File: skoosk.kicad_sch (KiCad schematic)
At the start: 99 parts, among them SW1 SW_Push, SW2 RotaryEncoder_Switch, U1 ProMicro

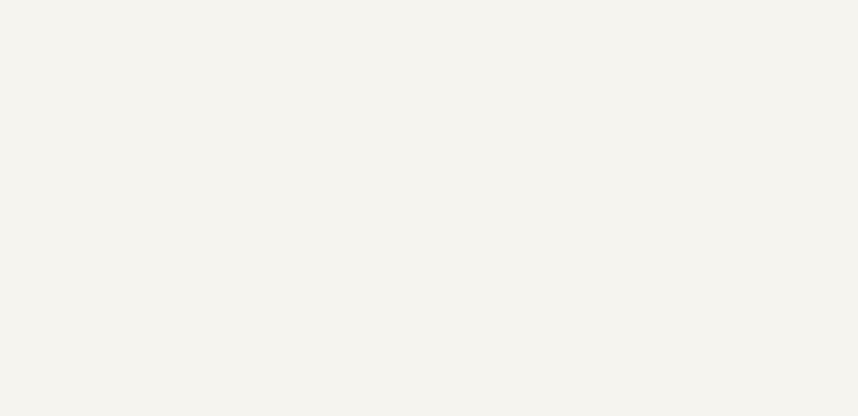
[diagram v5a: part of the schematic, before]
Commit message: mounting holes added
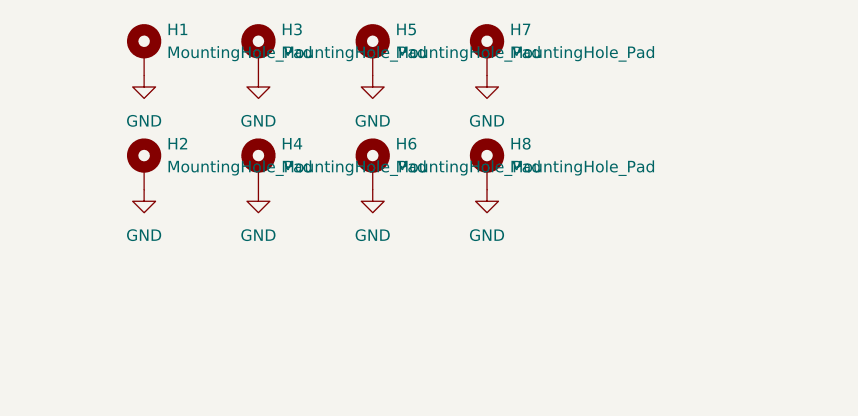
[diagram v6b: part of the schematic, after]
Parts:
- added H1, H2, H3, H4, H5, H6, H7, H8: MountingHole_Pad, MountingHole:MountingHole_2.7mm_M2.5_Pad, symbol Mechanical:MountingHole_Pad
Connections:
- net GND: now also H1.1, H2.1, H3.1, H4.1, H5.1, H6.1, H7.1, H8.1

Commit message: cleaned up pcb, switch & backplate
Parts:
- H1, H2, H3, H4, H5, H6, H7, H8: footprint MountingHole:MountingHole_2.7mm_M2.5_Pad -> MountingHole:MountingHole_2.2mm_M2_Pad
- Rrgb1: footprint Resistor_THT:R_Axial_DIN0204_L3.6mm_D1.6mm_P5.08mm_Horizontal -> Resistor_SMD:R_0603_1608Metric
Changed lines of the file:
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@@
       (effects (font (size 1.27 1.27)) (justify left))
     )
-    (property "Footprint" "MountingHole:MountingHole_2.7mm_M2.5_Pad" (id 2) (at 25.4 22.86 0)
+    (property "Footprint" "MountingHole:MountingHole_2.2mm_M2_Pad" (id 2) (at 25.4 22.86 0)
       (effects (font (size 1.27 1.27)) hide)
     )
@@
       (effects (font (size 1.27 1.27)) (justify left))
     )
-    (property "Footprint" "MountingHole:MountingHole_2.7mm_M2.5_Pad" (id 2) (at 50.8 22.86 0)
+    (property "Footprint" "MountingHole:MountingHole_2.2mm_M2_Pad" (id 2) (at 50.8 22.86 0)
       (effects (font (size 1.27 1.27)) hide)
     )
@@
       (effects (font (size 1.27 1.27)) (justify left))
     )
-    (property "Footprint" "MountingHole:MountingHole_2.7mm_M2.5_Pad" (id 2) (at 50.8 35.56 0)
+    (property "Footprint" "MountingHole:MountingHole_2.2mm_M2_Pad" (id 2) (at 50.8 35.56 0)
       (effects (font (size 1.27 1.27)) hide)
     )
@@
       (effects (font (size 1.27 1.27)) (justify left))
     )
-    (property "Footprint" "MountingHole:MountingHole_2.7mm_M2.5_Pad" (id 2) (at 38.1 35.56 0)
+    (property "Footprint" "MountingHole:MountingHole_2.2mm_M2_Pad" (id 2) (at 38.1 35.56 0)
       (effects (font (size 1.27 1.27)) hide)
     )
@@
       (effects (font (size 1.27 1.27)) (justify left))
     )
-    (property "Footprint" "MountingHole:MountingHole_2.7mm_M2.5_Pad" (id 2) (at 38.1 22.86 0)
+    (property "Footprint" "MountingHole:MountingHole_2.2mm_M2_Pad" (id 2) (at 38.1 22.86 0)
       (effects (font (size 1.27 1.27)) hide)
     )
@@
       (effects (font (size 1.27 1.27)) (justify left))
     )
-    (property "Footprint" "MountingHole:MountingHole_2.7mm_M2.5_Pad" (id 2) (at 63.5 22.86 0)
+    (property "Footprint" "MountingHole:MountingHole_2.2mm_M2_Pad" (id 2) (at 63.5 22.86 0)
       (effects (font (size 1.27 1.27)) hide)
     )
@@
       (effects (font (size 1.27 1.27)) (justify left))
     )
-    (property "Footprint" "MountingHole:MountingHole_2.7mm_M2.5_Pad" (id 2) (at 25.4 35.56 0)
+    (property "Footprint" "MountingHole:MountingHole_2.2mm_M2_Pad" (id 2) (at 25.4 35.56 0)
       (effects (font (size 1.27 1.27)) hide)
     )
@@
       (effects (font (size 1.27 1.27)) (justify left))
     )
-    (property "Footprint" "MountingHole:MountingHole_2.7mm_M2.5_Pad" (id 2) (at 63.5 35.56 0)
+    (property "Footprint" "MountingHole:MountingHole_2.2mm_M2_Pad" (id 2) (at 63.5 35.56 0)
       (effects (font (size 1.27 1.27)) hide)
     )
@@
       (effects (font (size 1.27 1.27)) (justify left))
     )
-    (property "Footprint" "Resistor_THT:R_Axial_DIN0204_L3.6mm_D1.6mm_P5.08mm_Horizontal" (id 2) (at 30.48 91.44 0)
+    (property "Footprint" "Resistor_SMD:R_0603_1608Metric" (id 2) (at 30.48 91.44 0)
       (effects (font (size 1.27 1.27)) hide)
     )
@@
     )
     (path "/1f47bf57-554a-4b3f-afe2-fbac827e2ba5"
-      (reference "H1") (unit 1) (value "MountingHole_Pad") (footprint "MountingHole:MountingHole_2.7mm_M2.5_Pad")
+      (reference "H1") (unit 1) (value "MountingHole_Pad") (footprint "MountingHole:MountingHole_2.2mm_M2_Pad")
     )
     (path "/af553349-715c-4608-b748-a1575ed68db3"
-      (reference "H2") (unit 1) (value "MountingHole_Pad") (footprint "MountingHole:MountingHole_2.7mm_M2.5_Pad")
+      (reference "H2") (unit 1) (value "MountingHole_Pad") (footprint "MountingHole:MountingHole_2.2mm_M2_Pad")
     )
     (path "/43888ca5-6957-4322-affa-2eb630f8517a"
-      (reference "H3") (unit 1) (value "MountingHole_Pad") (footprint "MountingHole:MountingHole_2.7mm_M2.5_Pad")
+      (reference "H3") (unit 1) (value "MountingHole_Pad") (footprint "MountingHole:MountingHole_2.2mm_M2_Pad")
     )
     (path "/3a0fec70-6df6-40fa-9366-eaf0a7aee334"
-      (reference "H4") (unit 1) (value "MountingHole_Pad") (footprint "MountingHole:MountingHole_2.7mm_M2.5_Pad")
+      (reference "H4") (unit 1) (value "MountingHole_Pad") (footprint "MountingHole:MountingHole_2.2mm_M2_Pad")
     )
     (path "/1f6c162c-0a68-4804-9c9c-5335247520ca"
-      (reference "H5") (unit 1) (value "MountingHole_Pad") (footprint "MountingHole:MountingHole_2.7mm_M2.5_Pad")
+      (reference "H5") (unit 1) (value "MountingHole_Pad") (footprint "MountingHole:MountingHole_2.2mm_M2_Pad")
     )
     (path "/2d647da6-4f5e-4e29-a307-e13c751eca0d"
-      (reference "H6") (unit 1) (value "MountingHole_Pad") (footprint "MountingHole:MountingHole_2.7mm_M2.5_Pad")
+      (reference "H6") (unit 1) (value "MountingHole_Pad") (footprint "MountingHole:MountingHole_2.2mm_M2_Pad")
     )
     (path "/8cca7ba2-0d01-424b-8f1c-53c92d666080"
-      (reference "H7") (unit 1) (value "MountingHole_Pad") (footprint "MountingHole:MountingHole_2.7mm_M2.5_Pad")
+      (reference "H7") (unit 1) (value "MountingHole_Pad") (footprint "MountingHole:MountingHole_2.2mm_M2_Pad")
     )
     (path "/d8d489d2-f21b-44ba-ae7f-430713468fdb"
-      (reference "H8") (unit 1) (value "MountingHole_Pad") (footprint "MountingHole:MountingHole_2.7mm_M2.5_Pad")
+      (reference "H8") (unit 1) (value "MountingHole_Pad") (footprint "MountingHole:MountingHole_2.2mm_M2_Pad")
     )
     (path "/06d6f48f-e469-4354-9f3f-73c3c7e47130"
@@
     )
     (path "/fbc2eaac-d9a0-45ae-9516-ef1321b60b11"
-      (reference "Rrgb1") (unit 1) (value "R_Small") (footprint "Resistor_THT:R_Axial_DIN0204_L3.6mm_D1.6mm_P5.08mm_Horizontal")
+      (reference "Rrgb1") (unit 1) (value "R_Small") (footprint "Resistor_SMD:R_0603_1608Metric")
     )
     (path "/20935e79-de43-4582-abe1-b13b50757846"

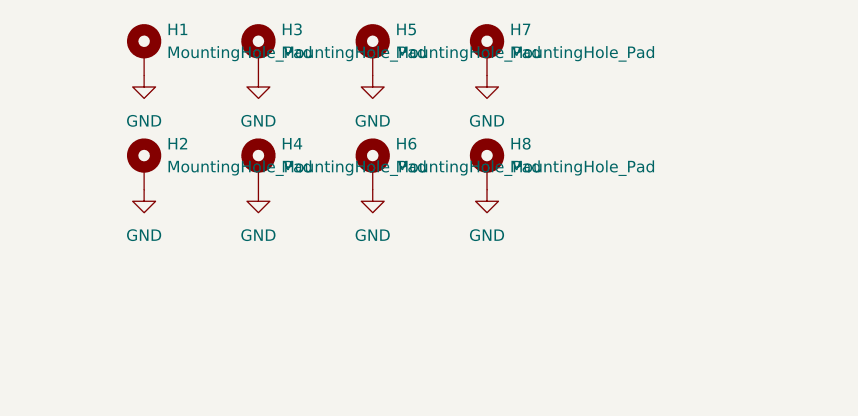
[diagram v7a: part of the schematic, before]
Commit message: cleaning up
changed pcb size, for mounting
flipped stabs on plate and pcb
changed clearance on copper fill
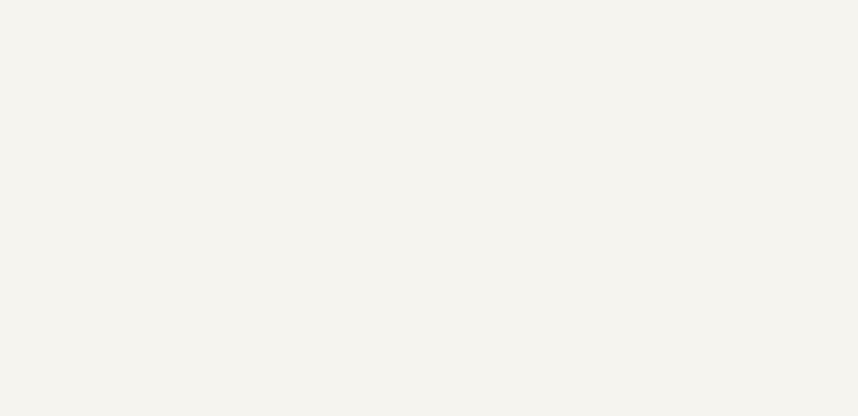
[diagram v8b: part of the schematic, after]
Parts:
- removed H1, H2, H3, H4, H5, H6, H7, H8: MountingHole_Pad, MountingHole:MountingHole_2.2mm_M2_Pad, symbol Mechanical:MountingHole_Pad
- MX40, MX41: footprint MX_Only:MXOnly-3U-NoLED -> MX_Only:MXOnly-3U-ReversedStabilizers-NoLED
